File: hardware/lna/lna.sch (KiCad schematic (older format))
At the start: 6 parts, among them J1 142-0701-801, J2 142-0701-801, U1 BGU7007,115

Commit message: completed schematic and laid out PCB
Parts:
- removed U1: BGU7007,115, BGU7007_115:PSON50P100X145X50-6N, symbol BGU7007_115:BGU7007,115
- added D1: Bi_ESD_Diode, lna:SOIC-2, symbol lna-rescue:Bi_ESD_Diode
- added U1: BGU8009, Package_TO_SOT_SMD:XSON-NXP-6, symbol lna-rescue:BGU8009
- J1, J2: symbol dk_Coaxial-Connectors-RF:142-0701-801 -> lna-rescue:142-0701-801-dk_Coaxial-Connectors-RF
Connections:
- net labels removed: GND
- wire segments 20 -> 22
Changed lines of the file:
@@
 EESchema Schematic File Version 4
+LIBS:lna-cache
 EELAYER 30 0
 EELAYER END
@@
 	0    -1   -1   0
 $EndComp
-$Comp
-L power:GND #PWR01
-U 1 1 5D69F118
-P 5050 3400
-F 0 "#PWR01" H 5050 3150 50  0001 C CNN
-F 1 "GND" H 5055 3227 50  0000 C CNN
-F 2 "" H 5050 3400 50  0001 C CNN
-F 3 "" H 5050 3400 50  0001 C CNN
-	1    5050 3400
-	1    0    0    -1
-$EndComp
 Wire Wire Line
 	7600 3850 6900 3850
@@
 	5050 3200 5050 3400
 $Comp
-L dk_Coaxial-Connectors-RF:142-0701-801 J1
+L lna-rescue:142-0701-801-dk_Coaxial-Connectors-RF J1
 U 1 1 5D6A8AB5
 P 4100 3850
@@
 $EndComp
 $Comp
-L dk_Coaxial-Connectors-RF:142-0701-801 J2
+L lna-rescue:142-0701-801-dk_Coaxial-Connectors-RF J2
 U 1 1 5D6AD89F
 P 7800 3850
@@
 L power:GNDA #PWR0101
 U 1 1 5D6B5D30
-P 7800 4250
-F 0 "#PWR0101" H 7800 4000 50  0001 C CNN
-F 1 "GNDA" H 7805 4077 50  0000 C CNN
-F 2 "" H 7800 4250 50  0001 C CNN
-F 3 "" H 7800 4250 50  0001 C CNN
-	1    7800 4250
-	1    0    0    -1
-$EndComp
+P 7800 4650
+F 0 "#PWR0101" H 7800 4400 50  0001 C CNN
+F 1 "GNDA" H 7805 4477 50  0000 C CNN
+F 2 "" H 7800 4650 50  0001 C CNN
+F 3 "" H 7800 4650 50  0001 C CNN
+	1    7800 4650
+	1    0    0    -1
+$EndComp
+Wire Wire Line
+	7800 4650 7800 4050
+Connection ~ 6900 3850
+Wire Wire Line
+	5650 3200 5750 3200
+Connection ~ 5950 3200
+Wire Wire Line
+	5950 3200 6500 3200
+Connection ~ 5750 3200
+Wire Wire Line
+	5750 3200 5950 3200
+$Comp
+L lna-rescue:BGU8009 U1
+U 1 1 5D6DBAD8
+P 5850 3850
+F 0 "U1" H 6344 3921 50  0000 L CNN
+F 1 "BGU8009" H 6344 3830 50  0000 L CNN
+F 2 "Package_TO_SOT_SMD:XSON-NXP-6" H 5850 3850 50  0001 C CNN
+F 3 "" H 5850 3850 50  0001 C CNN
+	1    5850 3850
+	1    0    0    -1
+$EndComp
+Wire Wire Line
+	5950 3350 5950 3200
+Wire Wire Line
+	5750 3350 5750 3200
+Wire Wire Line
+	5950 4300 5950 4450
+Wire Wire Line
+	5950 4450 5750 4450
+Wire Wire Line
+	5750 4450 5750 4300
+Connection ~ 5950 4450
+Wire Wire Line
+	5950 4450 5950 4650
+Wire Wire Line
+	6300 3850 6900 3850
+Wire Wire Line
+	4900 3850 5450 3850
+$Comp
+L lna-rescue:Bi_ESD_Diode D1
+U 1 1 5D6E5A3B
+P 6900 4400
+F 0 "D1" V 6829 4503 50  0000 L CNN
+F 1 "Bi_ESD_Diode" V 6920 4503 50  0000 L CNN
+F 2 "lna:SOIC-2" H 6900 4400 50  0001 C CNN
+F 3 "" H 6900 4400 50  0001 C CNN
+	1    6900 4400
+	0    1    1    0
+$EndComp
+$Comp
+L power:GNDA #PWR02
+U 1 1 5D6E5F67
+P 6900 4650
+F 0 "#PWR02" H 6900 4400 50  0001 C CNN
+F 1 "GNDA" H 6905 4477 50  0000 C CNN
+F 2 "" H 6900 4650 50  0001 C CNN
+F 3 "" H 6900 4650 50  0001 C CNN
+	1    6900 4650
+	1    0    0    -1
+$EndComp
+Wire Wire Line
+	6900 4650 6900 4600
+Wire Wire Line
+	6900 4150 6900 3850
+Wire Wire Line
+	4100 4200 4100 4050
 $Comp
 L power:GNDA #PWR0102
@@
 	1    0    0    -1
 $EndComp
-Wire Wire Line
-	7800 4250 7800 4050
-Wire Wire Line
-	4100 4200 4100 4050
-$Comp
-L BGU7007_115:BGU7007,115 U1
-U 1 1 5D6CB740
-P 5850 3850
-F 0 "U1" H 6394 3896 50  0000 L CNN
-F 1 "BGU7007,115" H 6394 3805 50  0000 L CNN
-F 2 "BGU7007_115:PSON50P100X145X50-6N" H 5850 3850 50  0001 L BNN
-F 3 "NXP USA" H 5850 3850 50  0001 L BNN
-F 4 "XFDFN-6 NXP Semiconductors" H 5850 3850 50  0001 L BNN "Field4"
-F 5 "BGU7007 Series 2.85 V 51 MHz Bw Low Noise Amplifier MMIC for GPS - XSON-6" H 5850 3850 50  0001 L BNN "Field5"
-F 6 "Unavailable" H 5850 3850 50  0001 L BNN "Field6"
-F 7 "BGU7007,115" H 5850 3850 50  0001 L BNN "Field7"
-F 8 "None" H 5850 3850 50  0001 L BNN "Field8"
-	1    5850 3850
-	1    0    0    -1
-$EndComp
-Wire Wire Line
-	6900 3850 6350 3850
-Connection ~ 6900 3850
-Wire Wire Line
-	5650 3200 5750 3200
-Wire Wire Line
-	5950 3450 5950 3200
-Connection ~ 5950 3200
-Wire Wire Line
-	5950 3200 6500 3200
-Wire Wire Line
-	5750 3450 5750 3200
-Connection ~ 5750 3200
-Wire Wire Line
-	5750 3200 5950 3200
-Wire Wire Line
-	5350 3850 4900 3850
-Wire Wire Line
-	5950 4250 5950 4450
-Wire Wire Line
-	5750 4250 5750 4450
-Wire Wire Line
-	5750 4450 5950 4450
-Connection ~ 5950 4450
-Wire Wire Line
-	5950 4450 5950 4650
+$Comp
+L power:GNDA #PWR?
+U 1 1 5D6EE6A7
+P 5050 3400
+F 0 "#PWR?" H 5050 3150 50  0001 C CNN
+F 1 "GNDA" H 5055 3227 50  0000 C CNN
+F 2 "" H 5050 3400 50  0001 C CNN
+F 3 "" H 5050 3400 50  0001 C CNN
+	1    5050 3400
+	1    0    0    -1
+$EndComp
 $EndSCHEMATC

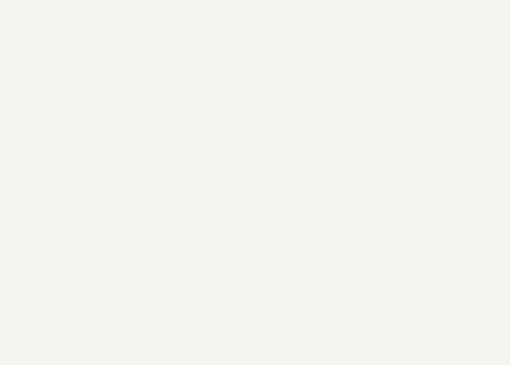
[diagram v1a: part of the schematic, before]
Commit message: changed connectors and added 3d stuff
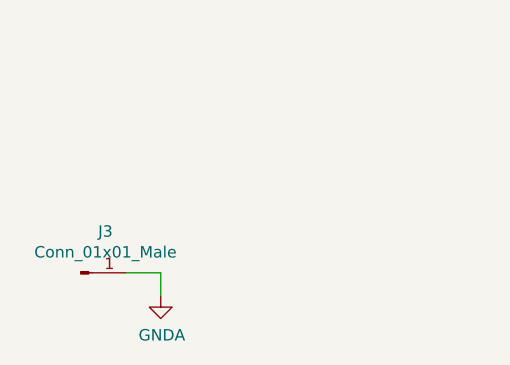
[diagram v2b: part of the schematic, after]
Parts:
- added J3: Conn_01x01_Male, RF_Shielding:Laird_Technologies_BMI-S-101_13.66x12.70mm, symbol Connector:Conn_01x01_Male
- J1, J2: footprint Connector_Coaxial:SMA_Amphenol_132289_EdgeMount -> Connector_Coaxial:SMA_Amphenol_132134_Vertical
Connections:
- net GNDA: now also J3.1 (Pin_1)
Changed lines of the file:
@@
 F 0 "J1" H 4178 4075 50  0000 C CNN
 F 1 "142-0701-801" H 4178 3984 50  0000 C CNN
-F 2 "Connector_Coaxial:SMA_Amphenol_132289_EdgeMount" H 4300 4050 60  0001 L CNN
+F 2 "Connector_Coaxial:SMA_Amphenol_132134_Vertical" H 4300 4050 60  0001 L CNN
 F 3 "http://www.belfuse.com/resources/Johnson/drawings/dr-1420701801.pdf" H 4300 4150 60  0001 L CNN
 F 4 "J502-ND" H 4300 4250 60  0001 L CNN "Digi-Key_PN"
@@
 F 0 "J2" H 7712 3818 50  0000 R CNN
 F 1 "142-0701-801" H 7712 3727 50  0000 R CNN
-F 2 "Connector_Coaxial:SMA_Amphenol_132289_EdgeMount" H 8000 4050 60  0001 L CNN
+F 2 "Connector_Coaxial:SMA_Amphenol_132134_Vertical" H 8000 4050 60  0001 L CNN
 F 3 "http://www.belfuse.com/resources/Johnson/drawings/dr-1420701801.pdf" H 8000 4150 60  0001 L CNN
 F 4 "J502-ND" H 8000 4250 60  0001 L CNN "Digi-Key_PN"
@@
 $EndComp
 $Comp
-L power:GNDA #PWR?
+L power:GNDA #PWR0103
 U 1 1 5D6EE6A7
 P 5050 3400
-F 0 "#PWR?" H 5050 3150 50  0001 C CNN
+F 0 "#PWR0103" H 5050 3150 50  0001 C CNN
 F 1 "GNDA" H 5055 3227 50  0000 C CNN
 F 2 "" H 5050 3400 50  0001 C CNN
@@
 	1    0    0    -1
 $EndComp
+$Comp
+L Connector:Conn_01x01_Male J3
+U 1 1 5D6F996D
+P 2000 6650
+F 0 "J3" H 2108 6831 50  0000 C CNN
+F 1 "Conn_01x01_Male" H 2108 6740 50  0000 C CNN
+F 2 "RF_Shielding:Laird_Technologies_BMI-S-101_13.66x12.70mm" H 2000 6650 50  0001 C CNN
+F 3 "~" H 2000 6650 50  0001 C CNN
+	1    2000 6650
+	1    0    0    -1
+$EndComp
+$Comp
+L power:GNDA #PWR0104
+U 1 1 5D6F2F18
+P 2350 6750
+F 0 "#PWR0104" H 2350 6500 50  0001 C CNN
+F 1 "GNDA" H 2355 6577 50  0000 C CNN
+F 2 "" H 2350 6750 50  0001 C CNN
+F 3 "" H 2350 6750 50  0001 C CNN
+	1    2350 6750
+	1    0    0    -1
+$EndComp
+Wire Wire Line
+	2200 6650 2350 6650
+Wire Wire Line
+	2350 6650 2350 6750
 $EndSCHEMATC

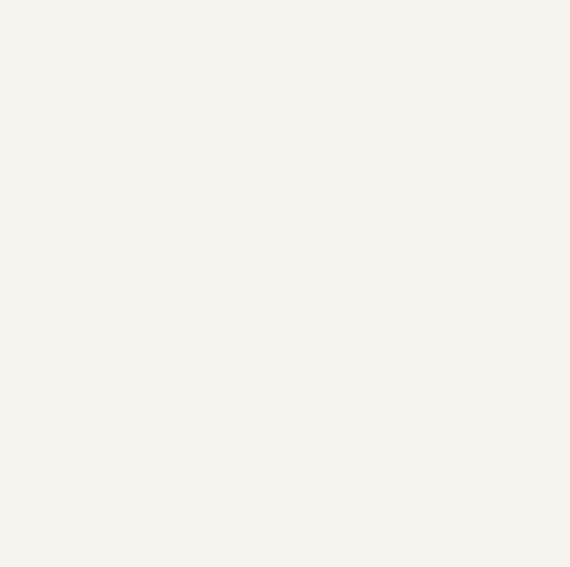
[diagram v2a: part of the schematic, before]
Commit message: Add shield and mounting holes
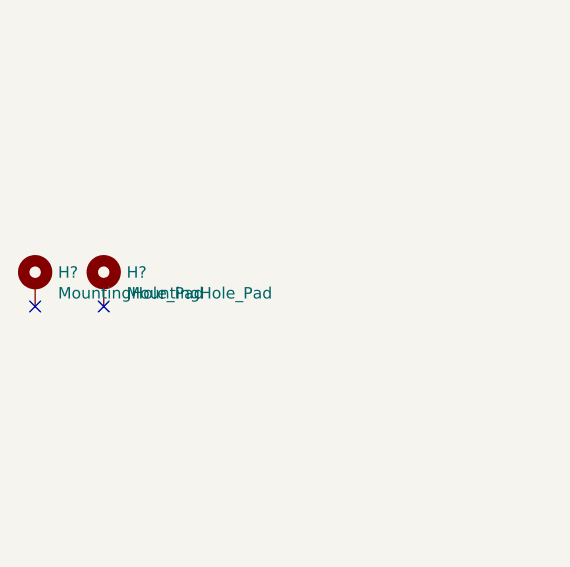
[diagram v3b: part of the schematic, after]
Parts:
- added H? (x2): MountingHole_Pad, symbol Mechanical:MountingHole_Pad
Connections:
- no-connect marks 0 -> 2
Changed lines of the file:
@@
 Wire Wire Line
 	2350 6650 2350 6750
+$Comp
+L Mechanical:MountingHole_Pad H?
+U 1 1 5D70E3CC
+P 950 4750
+F 0 "H?" H 1050 4799 50  0000 L CNN
+F 1 "MountingHole_Pad" H 1050 4708 50  0000 L CNN
+F 2 "" H 950 4750 50  0001 C CNN
+F 3 "~" H 950 4750 50  0001 C CNN
+	1    950  4750
+	1    0    0    -1
+$EndComp
+$Comp
+L Mechanical:MountingHole_Pad H?
+U 1 1 5D70EDF1
+P 1250 4750
+F 0 "H?" H 1350 4799 50  0000 L CNN
+F 1 "MountingHole_Pad" H 1350 4708 50  0000 L CNN
+F 2 "" H 1250 4750 50  0001 C CNN
+F 3 "~" H 1250 4750 50  0001 C CNN
+	1    1250 4750
+	1    0    0    -1
+$EndComp
+NoConn ~ 950  4850
+NoConn ~ 1250 4850
 $EndSCHEMATC

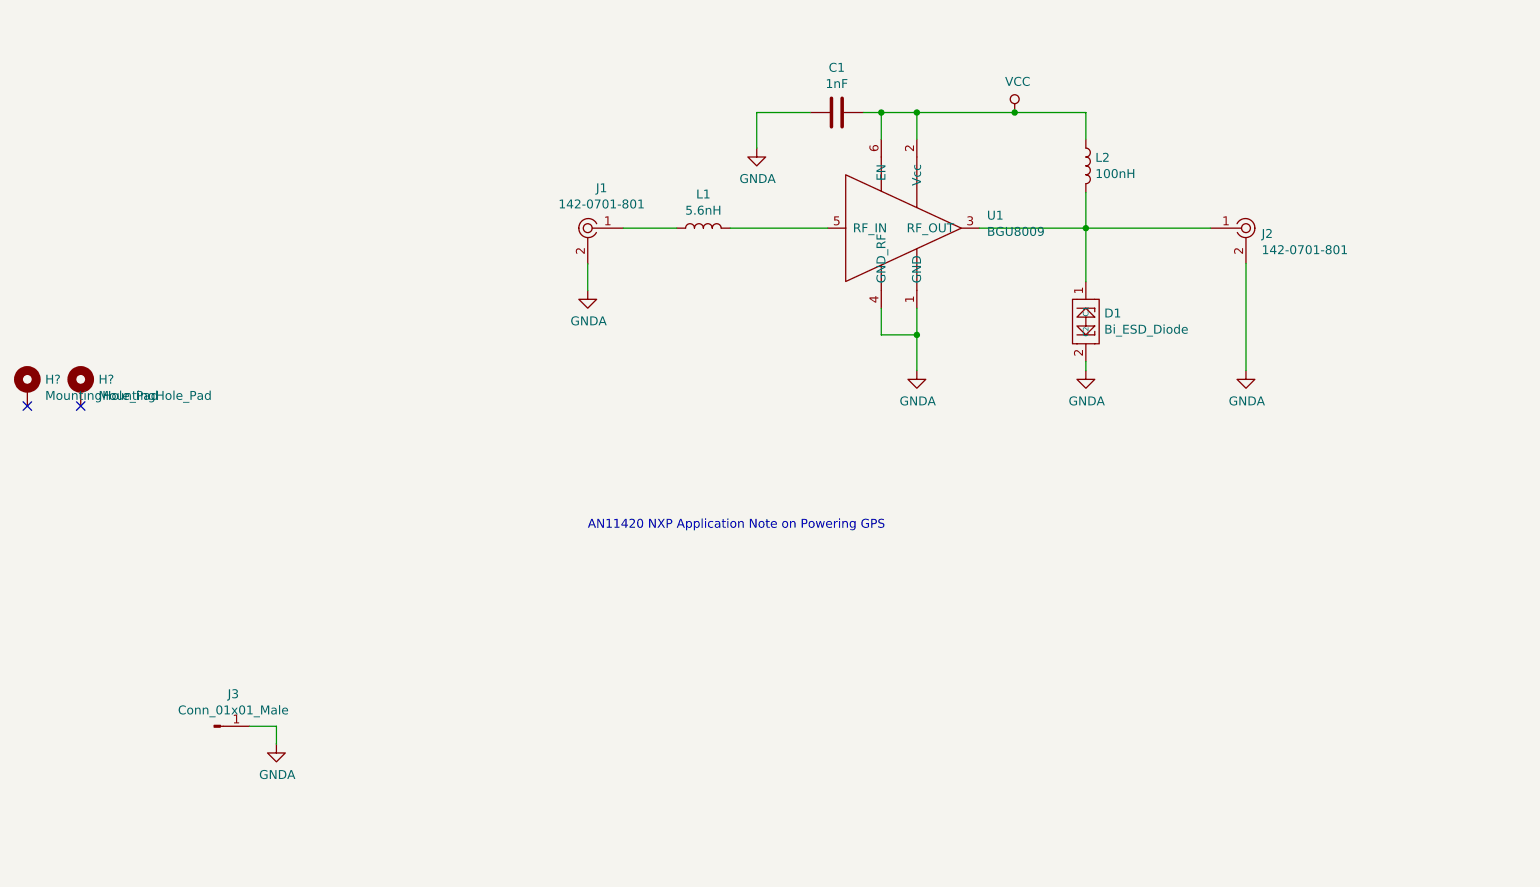
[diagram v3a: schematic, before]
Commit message: Preliminary radio module schematic
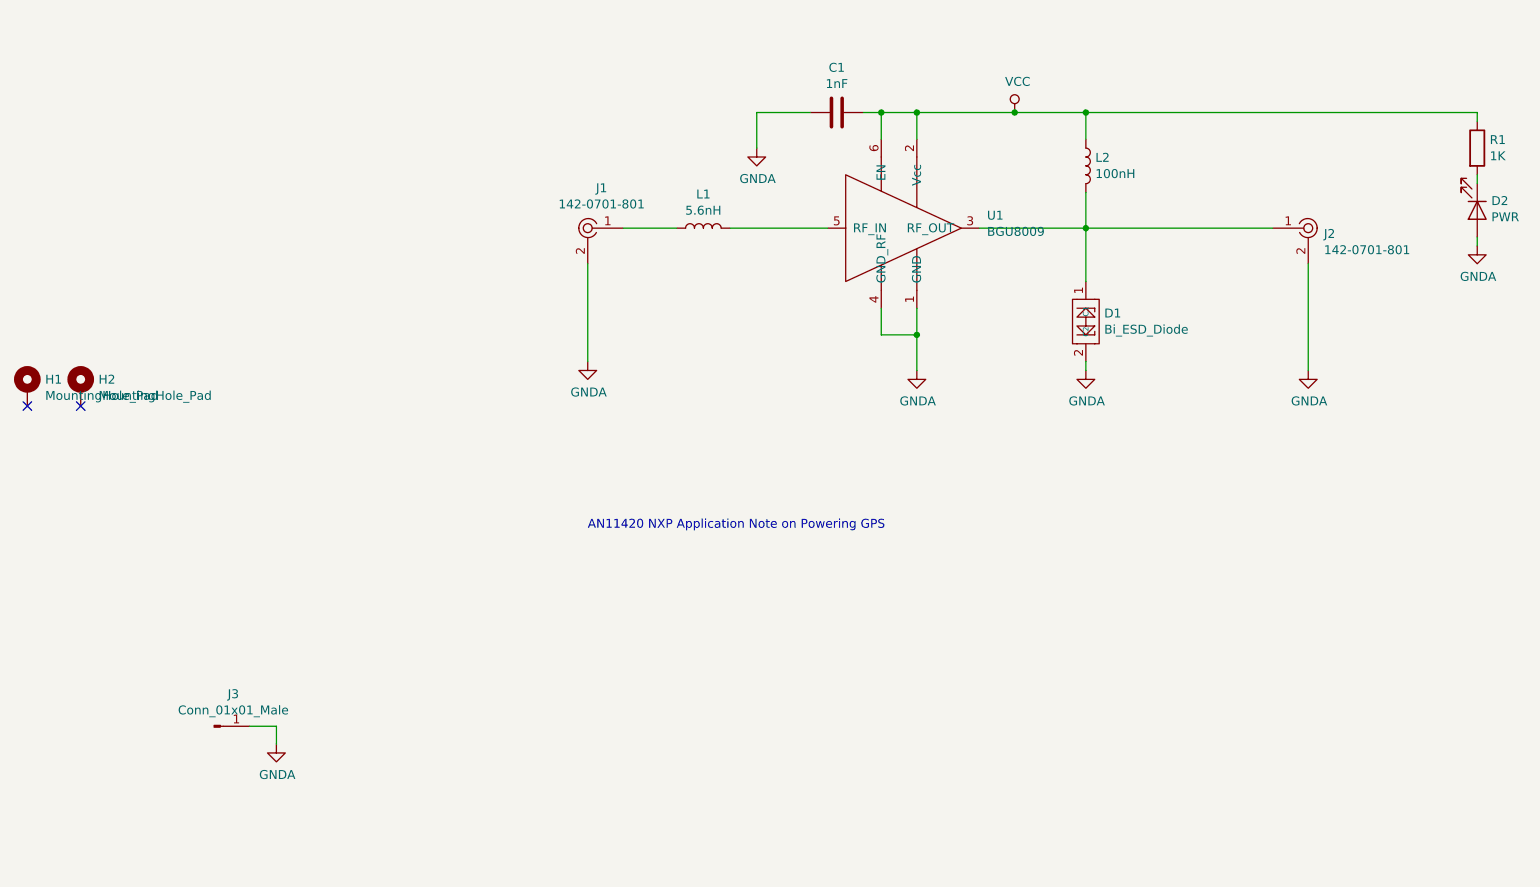
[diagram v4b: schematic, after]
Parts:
- added D2: PWR, LED_SMD:LED_0603_1608Metric_Pad1.05x0.95mm_HandSolder, symbol Device:LED
- added R1: 1K, Resistor_SMD:R_0603_1608Metric_Pad1.05x0.95mm_HandSolder, symbol Device:R
- H1, H2: renamed from H?; footprint (none) -> MountingHole:MountingHole_3.2mm_M3_Pad_Via
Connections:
- net GNDA: now also D2.2 (A)
- net VCC: now also R1.1
- new net: D2.1 (K), R1.2
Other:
- moved on the sheet: J2
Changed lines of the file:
@@
 $EndComp
-Wire Wire Line
-	7600 3850 6900 3850
 Wire Wire Line
 	6900 3650 6900 3850
@@
 L lna-rescue:142-0701-801-dk_Coaxial-Connectors-RF J2
 U 1 1 5D6AD89F
-P 7800 3850
-F 0 "J2" H 7712 3818 50  0000 R CNN
-F 1 "142-0701-801" H 7712 3727 50  0000 R CNN
-F 2 "Connector_Coaxial:SMA_Amphenol_132134_Vertical" H 8000 4050 60  0001 L CNN
-F 3 "http://www.belfuse.com/resources/Johnson/drawings/dr-1420701801.pdf" H 8000 4150 60  0001 L CNN
-F 4 "J502-ND" H 8000 4250 60  0001 L CNN "Digi-Key_PN"
-F 5 "142-0701-801" H 8000 4350 60  0001 L CNN "MPN"
-F 6 "Connectors, Interconnects" H 8000 4450 60  0001 L CNN "Category"
-F 7 "Coaxial Connectors (RF)" H 8000 4550 60  0001 L CNN "Family"
-F 8 "http://www.belfuse.com/resources/Johnson/drawings/dr-1420701801.pdf" H 8000 4650 60  0001 L CNN "DK_Datasheet_Link"
-F 9 "/product-detail/en/cinch-connectivity-solutions-johnson/142-0701-801/J502-ND/35280" H 8000 4750 60  0001 L CNN "DK_Detail_Page"
-F 10 "CONN SMA JACK STR 50OHM EDGE MNT" H 8000 4850 60  0001 L CNN "Description"
-F 11 "Cinch Connectivity Solutions Johnson" H 8000 4950 60  0001 L CNN "Manufacturer"
-F 12 "Active" H 8000 5050 60  0001 L CNN "Status"
-	1    7800 3850
+P 8150 3850
+F 0 "J2" H 8062 3818 50  0000 R CNN
+F 1 "142-0701-801" H 8062 3727 50  0000 R CNN
+F 2 "Connector_Coaxial:SMA_Amphenol_132134_Vertical" H 8350 4050 60  0001 L CNN
+F 3 "http://www.belfuse.com/resources/Johnson/drawings/dr-1420701801.pdf" H 8350 4150 60  0001 L CNN
+F 4 "J502-ND" H 8350 4250 60  0001 L CNN "Digi-Key_PN"
+F 5 "142-0701-801" H 8350 4350 60  0001 L CNN "MPN"
+F 6 "Connectors, Interconnects" H 8350 4450 60  0001 L CNN "Category"
+F 7 "Coaxial Connectors (RF)" H 8350 4550 60  0001 L CNN "Family"
+F 8 "http://www.belfuse.com/resources/Johnson/drawings/dr-1420701801.pdf" H 8350 4650 60  0001 L CNN "DK_Datasheet_Link"
+F 9 "/product-detail/en/cinch-connectivity-solutions-johnson/142-0701-801/J502-ND/35280" H 8350 4750 60  0001 L CNN "DK_Detail_Page"
+F 10 "CONN SMA JACK STR 50OHM EDGE MNT" H 8350 4850 60  0001 L CNN "Description"
+F 11 "Cinch Connectivity Solutions Johnson" H 8350 4950 60  0001 L CNN "Manufacturer"
+F 12 "Active" H 8350 5050 60  0001 L CNN "Status"
+	1    8150 3850
 	-1   0    0    -1
 $EndComp
@@
 L power:GNDA #PWR0101
 U 1 1 5D6B5D30
-P 7800 4650
-F 0 "#PWR0101" H 7800 4400 50  0001 C CNN
-F 1 "GNDA" H 7805 4477 50  0000 C CNN
-F 2 "" H 7800 4650 50  0001 C CNN
-F 3 "" H 7800 4650 50  0001 C CNN
-	1    7800 4650
-	1    0    0    -1
-$EndComp
-Wire Wire Line
-	7800 4650 7800 4050
+P 8150 4650
+F 0 "#PWR0101" H 8150 4400 50  0001 C CNN
+F 1 "GNDA" H 8155 4477 50  0000 C CNN
+F 2 "" H 8150 4650 50  0001 C CNN
+F 3 "" H 8150 4650 50  0001 C CNN
+	1    8150 4650
+	1    0    0    -1
+$EndComp
+Wire Wire Line
+	8150 4650 8150 4050
 Connection ~ 6900 3850
 Wire Wire Line
@@
 	6900 4150 6900 3850
 Wire Wire Line
-	4100 4200 4100 4050
+	4100 4600 4100 4050
 $Comp
 L power:GNDA #PWR0102
 U 1 1 5D6B61DB
-P 4100 4200
-F 0 "#PWR0102" H 4100 3950 50  0001 C CNN
-F 1 "GNDA" H 4105 4027 50  0000 C CNN
-F 2 "" H 4100 4200 50  0001 C CNN
-F 3 "" H 4100 4200 50  0001 C CNN
-	1    4100 4200
+P 4100 4600
+F 0 "#PWR0102" H 4100 4350 50  0001 C CNN
+F 1 "GNDA" H 4105 4427 50  0000 C CNN
+F 2 "" H 4100 4600 50  0001 C CNN
+F 3 "" H 4100 4600 50  0001 C CNN
+	1    4100 4600
 	1    0    0    -1
 $EndComp
@@
 	2350 6650 2350 6750
 $Comp
-L Mechanical:MountingHole_Pad H?
+L Mechanical:MountingHole_Pad H1
 U 1 1 5D70E3CC
 P 950 4750
-F 0 "H?" H 1050 4799 50  0000 L CNN
+F 0 "H1" H 1050 4799 50  0000 L CNN
 F 1 "MountingHole_Pad" H 1050 4708 50  0000 L CNN
-F 2 "" H 950 4750 50  0001 C CNN
+F 2 "MountingHole:MountingHole_3.2mm_M3_Pad_Via" H 950 4750 50  0001 C CNN
 F 3 "~" H 950 4750 50  0001 C CNN
 	1    950  4750
@@
 $EndComp
 $Comp
-L Mechanical:MountingHole_Pad H?
+L Mechanical:MountingHole_Pad H2
 U 1 1 5D70EDF1
 P 1250 4750
-F 0 "H?" H 1350 4799 50  0000 L CNN
+F 0 "H2" H 1350 4799 50  0000 L CNN
 F 1 "MountingHole_Pad" H 1350 4708 50  0000 L CNN
-F 2 "" H 1250 4750 50  0001 C CNN
+F 2 "MountingHole:MountingHole_3.2mm_M3_Pad_Via" H 1250 4750 50  0001 C CNN
 F 3 "~" H 1250 4750 50  0001 C CNN
 	1    1250 4750
@@
 NoConn ~ 950  4850
 NoConn ~ 1250 4850
+$Comp
+L Device:LED D2
+U 1 1 5D9FB079
+P 9100 3750
+F 0 "D2" V 9047 3829 50  0000 L CNN
+F 1 "PWR" V 9138 3829 50  0000 L CNN
+F 2 "LED_SMD:LED_0603_1608Metric_Pad1.05x0.95mm_HandSolder" H 9100 3750 50  0001 C CNN
+F 3 "~" H 9100 3750 50  0001 C CNN
+	1    9100 3750
+	0    1    1    0
+$EndComp
+$Comp
+L Device:R R1
+U 1 1 5D9FC178
+P 9100 3400
+F 0 "R1" H 9170 3446 50  0000 L CNN
+F 1 "1K" H 9170 3355 50  0000 L CNN
+F 2 "Resistor_SMD:R_0603_1608Metric_Pad1.05x0.95mm_HandSolder" V 9030 3400 50  0001 C CNN
+F 3 "~" H 9100 3400 50  0001 C CNN
+	1    9100 3400
+	1    0    0    -1
+$EndComp
+$Comp
+L power:GNDA #PWR0105
+U 1 1 5DA0533E
+P 9100 3950
+F 0 "#PWR0105" H 9100 3700 50  0001 C CNN
+F 1 "GNDA" H 9105 3777 50  0000 C CNN
+F 2 "" H 9100 3950 50  0001 C CNN
+F 3 "" H 9100 3950 50  0001 C CNN
+	1    9100 3950
+	1    0    0    -1
+$EndComp
+Wire Wire Line
+	9100 3950 9100 3900
+Wire Wire Line
+	9100 3600 9100 3550
+Wire Wire Line
+	6900 3850 7950 3850
+Wire Wire Line
+	6900 3200 9100 3200
+Wire Wire Line
+	9100 3200 9100 3250
+Connection ~ 6900 3200
 $EndSCHEMATC
